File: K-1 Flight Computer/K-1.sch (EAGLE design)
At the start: 19 parts, among them IC1 BMP280, IC2 7805L, J1 1X2-3.5MM, J6 1X2-3.5MM, U1 MPU-6050-1

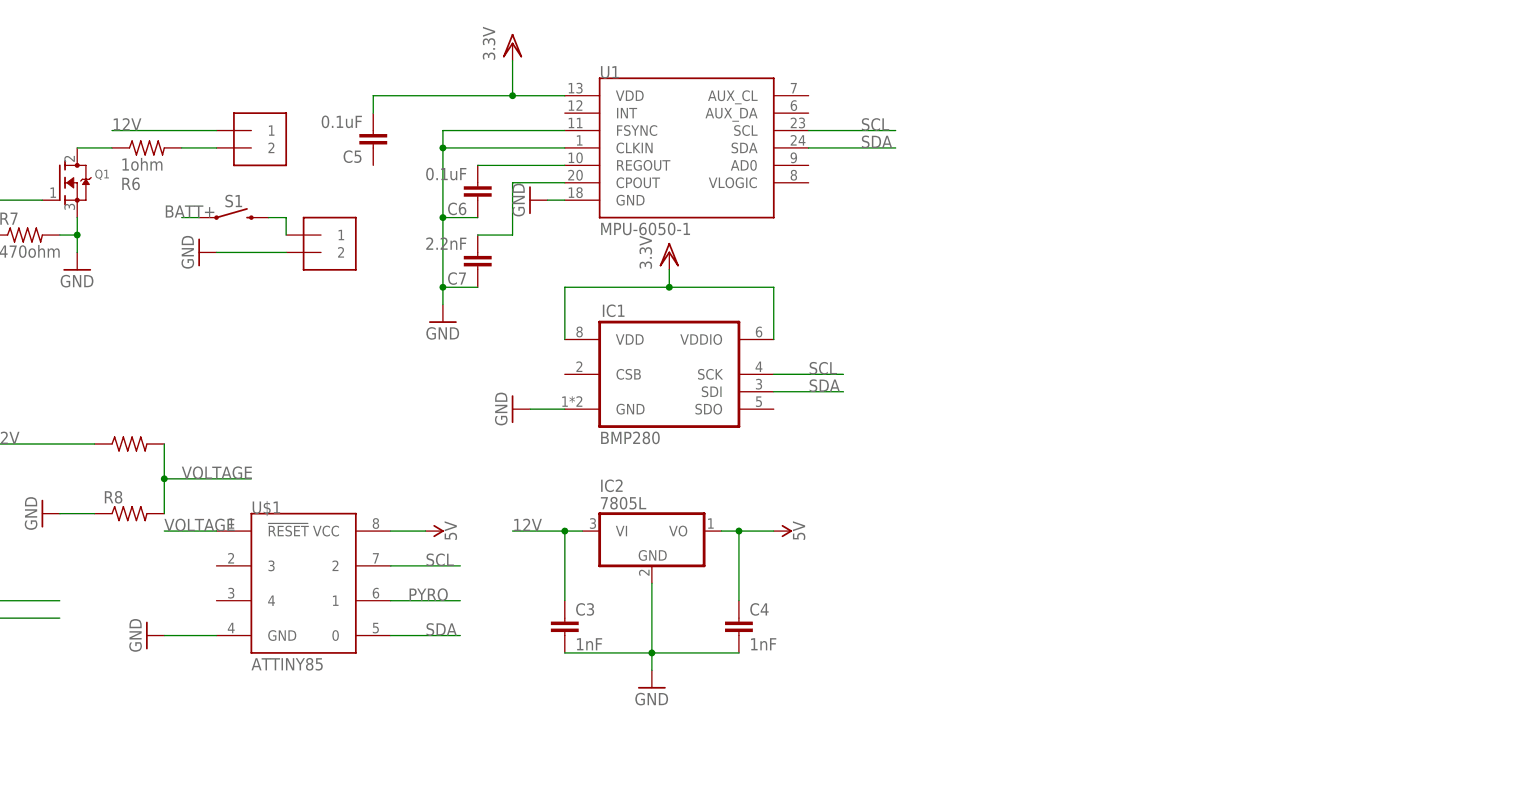
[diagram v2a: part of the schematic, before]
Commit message: Change MCU to STM32F103C8T7
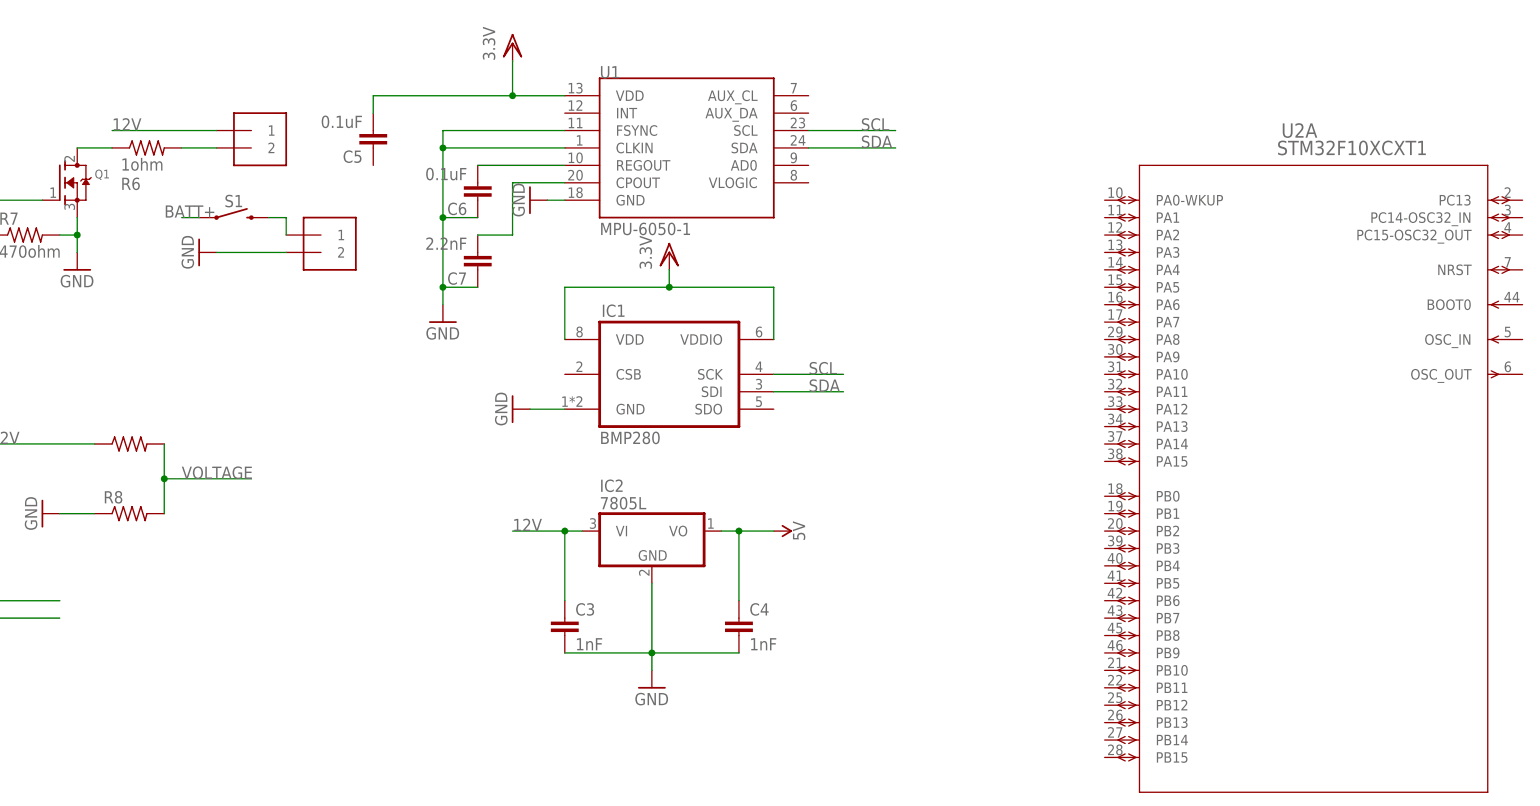
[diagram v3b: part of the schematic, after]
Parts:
- removed U$1: ATTINY85, attiny85:ATTINY85
- added U2: STM32F10XCXT1, STM32F103C8T7:STM32F10XCXT1
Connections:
- net 5V: no longer U$1.VCC
- net GND: no longer U$1.GND
- net PYRO: no longer U$1.1
- net SCL: no longer U$1.2
- net SDA: no longer U$1.0
- net VOLTAGE: no longer U$1.!RESET
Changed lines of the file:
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@@
 </classes>
 <parts>
-<part name="U$1" library="attiny85" deviceset="ATTINY85" device=""/>
 <part name="IC1" library="bosch-bmp280" deviceset="BMP280" device=""/>
 <part name="J1" library="adafruit" library_urn="urn:adsk.eagle:library:420" deviceset="1X2" device="-3.5MM" package3d_urn="urn:adsk.eagle:package:6240635/1"/>
@@
 <part name="R8" library="adafruit" library_urn="urn:adsk.eagle:library:420" deviceset="R-US_" device="0204/2V" package3d_urn="urn:adsk.eagle:package:6240630/1"/>
 <part name="GND8" library="supply1" library_urn="urn:adsk.eagle:library:371" deviceset="GND" device=""/>
-<part name="GND9" library="supply1" library_urn="urn:adsk.eagle:library:371" deviceset="GND" device=""/>
-<part name="SUPPLY2" library="SparkFun-PowerSymbols" library_urn="urn:adsk.eagle:library:530" deviceset="5V" device=""/>
 <part name="U1" library="Testing" deviceset="MPU-6050" device="-1"/>
 <part name="C3" library="capacitor-wima" library_urn="urn:adsk.eagle:library:116" deviceset="C" device="2,5-3" package3d_urn="urn:adsk.eagle:package:5436/1" value="1nF"/>
@@
 <part name="GND1" library="supply1" library_urn="urn:adsk.eagle:library:371" deviceset="GND" device=""/>
 <part name="S1" library="SparkFun-Switches" library_urn="urn:adsk.eagle:library:535" deviceset="MOMENTARY-SWITCH-SPST" device="-SMD-5.2-REDUNDANT" package3d_urn="urn:adsk.eagle:package:40167/1"/>
+<part name="U2" library="STM32F103C8T7" deviceset="STM32F10XCXT1" device=""/>
 </parts>
 <sheets>
@@
 </plain>
 <instances>
-<instance part="U$1" gate="G$1" x="142.24" y="78.74" smashed="yes">
-<attribute name="NAME" x="134.62" y="88.9" size="1.778" layer="95"/>
-<attribute name="VALUE" x="134.62" y="66.04" size="1.778" layer="96"/>
-</instance>
 <instance part="IC1" gate="G$1" x="195.58" y="109.22" smashed="yes">
 <attribute name="NAME" x="185.674" y="117.602" size="1.778" layer="95" font="vector"/>
@@
 <attribute name="VALUE" x="101.6" y="91.44" size="1.778" layer="96" rot="R270"/>
 </instance>
-<instance part="GND9" gate="1" x="119.38" y="71.12" smashed="yes" rot="R270">
-<attribute name="VALUE" x="116.84" y="73.66" size="1.778" layer="96" rot="R270"/>
-</instance>
-<instance part="SUPPLY2" gate="G$1" x="160.02" y="86.36" smashed="yes" rot="R270">
-<attribute name="VALUE" x="162.814" y="86.36" size="1.778" layer="96" rot="R270" align="bottom-center"/>
-</instance>
 <instance part="U1" gate="G$1" x="198.12" y="142.24" smashed="yes">
 <attribute name="NAME" x="185.42" y="152.4" size="1.778" layer="95"/>
@@
 <instance part="S1" gate="G$1" x="132.08" y="132.08" smashed="yes">
 <attribute name="NAME" x="132.08" y="133.604" size="1.778" layer="95" font="vector" align="bottom-center"/>
+</instance>
+<instance part="U2" gate="A" x="256.54" y="134.62" smashed="yes">
+<attribute name="NAME" x="284.8356" y="143.7386" size="2.0828" layer="95" ratio="6" rot="SR0"/>
+<attribute name="VALUE" x="284.2006" y="141.1986" size="2.0828" layer="96" ratio="6" rot="SR0"/>
 </instance>
 </instances>
@@
 <pinref part="GND8" gate="1" pin="GND"/>
 <wire x1="111.76" y1="88.9" x2="106.68" y2="88.9" width="0.1524" layer="91"/>
-</segment>
-<segment>
-<pinref part="U$1" gate="G$1" pin="GND"/>
-<wire x1="129.54" y1="71.12" x2="121.92" y2="71.12" width="0.1524" layer="91"/>
-<pinref part="GND9" gate="1" pin="GND"/>
 </segment>
 <segment>
@@
 <pinref part="C4" gate="G$1" pin="1"/>
 </segment>
-<segment>
-<pinref part="U$1" gate="G$1" pin="VCC"/>
-<pinref part="SUPPLY2" gate="G$1" pin="5V"/>
-<wire x1="154.94" y1="86.36" x2="160.02" y2="86.36" width="0.1524" layer="91"/>
-</segment>
 </net>
 <net name="N$4" class="0">
@@
 <label x="86.36" y="134.62" size="1.778" layer="95"/>
 </segment>
-<segment>
-<pinref part="U$1" gate="G$1" pin="1"/>
-<wire x1="154.94" y1="76.2" x2="165.1" y2="76.2" width="0.1524" layer="91"/>
-<label x="157.48" y="76.2" size="1.778" layer="95"/>
-</segment>
 </net>
 <net name="VOLTAGE" class="0">
@@
 <label x="124.46" y="93.98" size="1.778" layer="95"/>
 </segment>
-<segment>
-<pinref part="U$1" gate="G$1" pin="!RESET"/>
-<wire x1="129.54" y1="86.36" x2="121.92" y2="86.36" width="0.1524" layer="91"/>
-<label x="121.92" y="86.36" size="1.778" layer="95"/>
-</segment>
 </net>
 <net name="N$12" class="0">
@@
 </segment>
 <segment>
-<pinref part="U$1" gate="G$1" pin="0"/>
-<wire x1="154.94" y1="71.12" x2="165.1" y2="71.12" width="0.1524" layer="91"/>
-<label x="160.02" y="71.12" size="1.778" layer="95"/>
-</segment>
-<segment>
 <pinref part="U1" gate="G$1" pin="SDA"/>
 <wire x1="215.9" y1="142.24" x2="228.6" y2="142.24" width="0.1524" layer="91"/>
@@
 </segment>
 <segment>
-<pinref part="U$1" gate="G$1" pin="2"/>
-<wire x1="154.94" y1="81.28" x2="165.1" y2="81.28" width="0.1524" layer="91"/>
-<label x="160.02" y="81.28" size="1.778" layer="95"/>
-</segment>
-<segment>

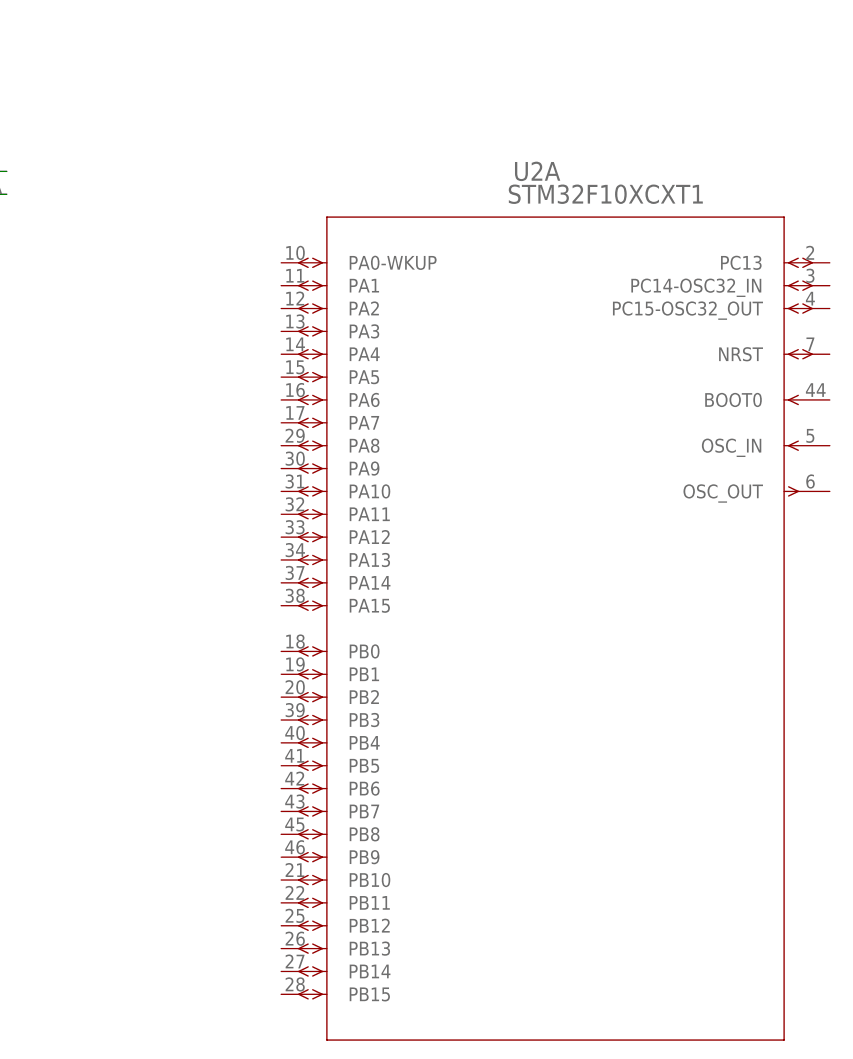
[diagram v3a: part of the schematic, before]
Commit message: Added custom MPU Eagle Library
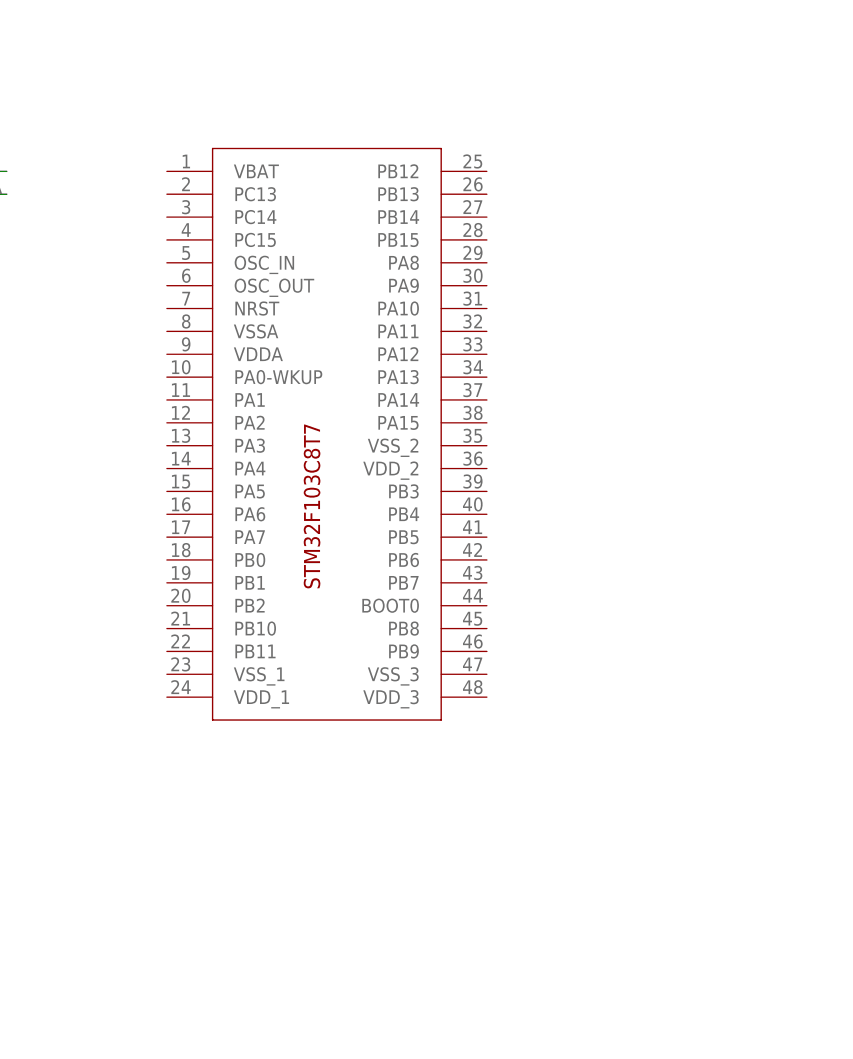
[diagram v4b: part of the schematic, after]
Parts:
- removed U2: STM32F10XCXT1, STM32F103C8T7:STM32F10XCXT1
- added U$1: STM32F103C8T7, STM32F103C8T7:STM32F103C8T7
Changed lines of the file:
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@@
 <part name="GND1" library="supply1" library_urn="urn:adsk.eagle:library:371" deviceset="GND" device=""/>
 <part name="S1" library="SparkFun-Switches" library_urn="urn:adsk.eagle:library:535" deviceset="MOMENTARY-SWITCH-SPST" device="-SMD-5.2-REDUNDANT" package3d_urn="urn:adsk.eagle:package:40167/1"/>
-<part name="U2" library="STM32F103C8T7" deviceset="STM32F10XCXT1" device=""/>
+<part name="U$1" library="STM32F103C8T7" deviceset="STM32F103C8T7" device=""/>
 </parts>
 <sheets>
@@
 <attribute name="NAME" x="132.08" y="133.604" size="1.778" layer="95" font="vector" align="bottom-center"/>
 </instance>
-<instance part="U2" gate="A" x="256.54" y="134.62" smashed="yes">
-<attribute name="NAME" x="284.8356" y="143.7386" size="2.0828" layer="95" ratio="6" rot="SR0"/>
-<attribute name="VALUE" x="284.2006" y="141.1986" size="2.0828" layer="96" ratio="6" rot="SR0"/>
-</instance>
+<instance part="U$1" gate="G$1" x="271.78" y="114.3" smashed="yes"/>
 </instances>
 <busses>

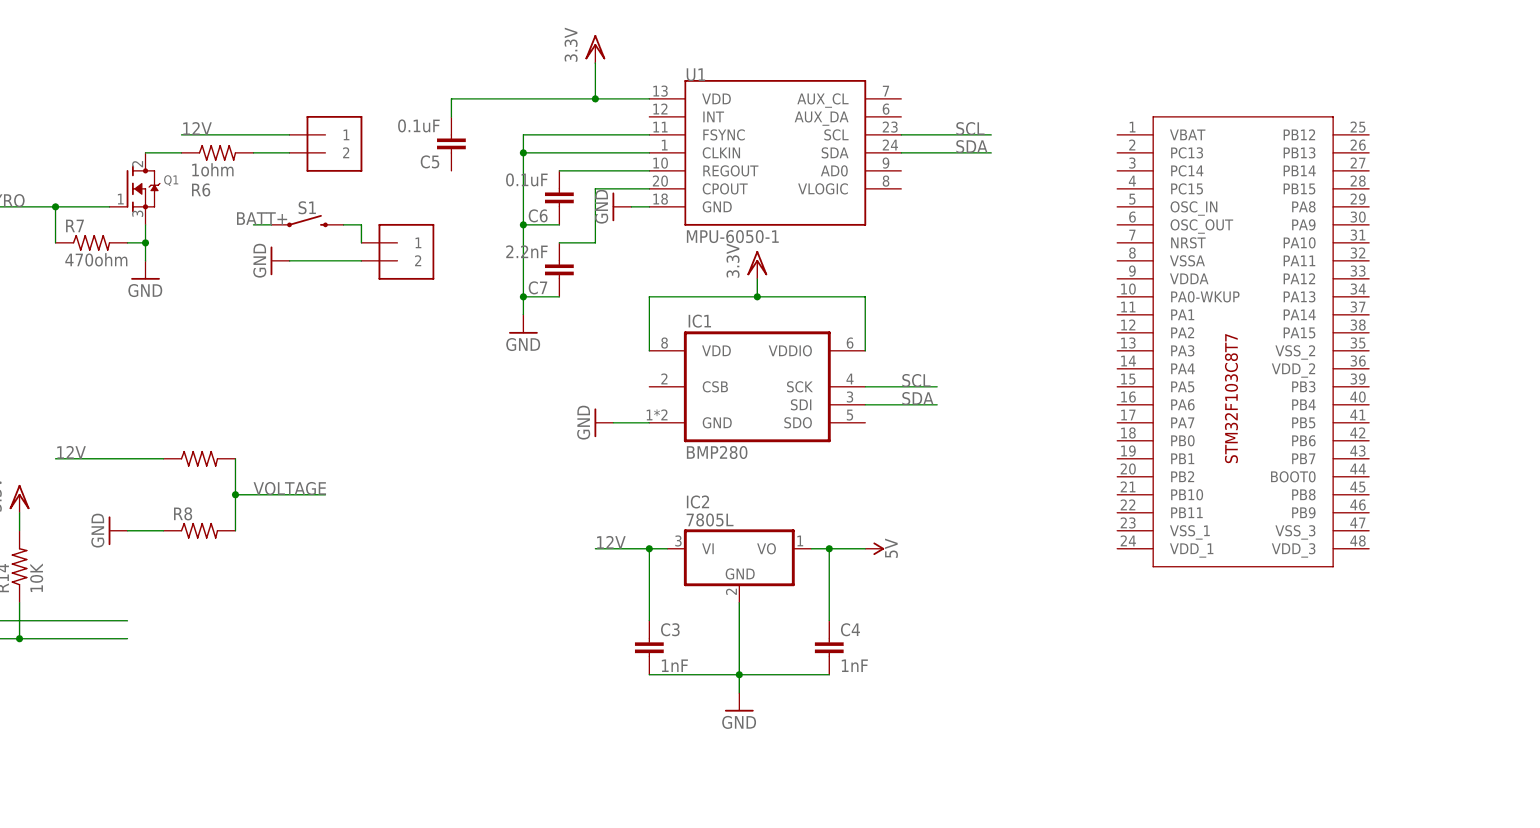
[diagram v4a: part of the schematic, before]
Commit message: Added W25Q32FV Memory Chip through SPI Protocol
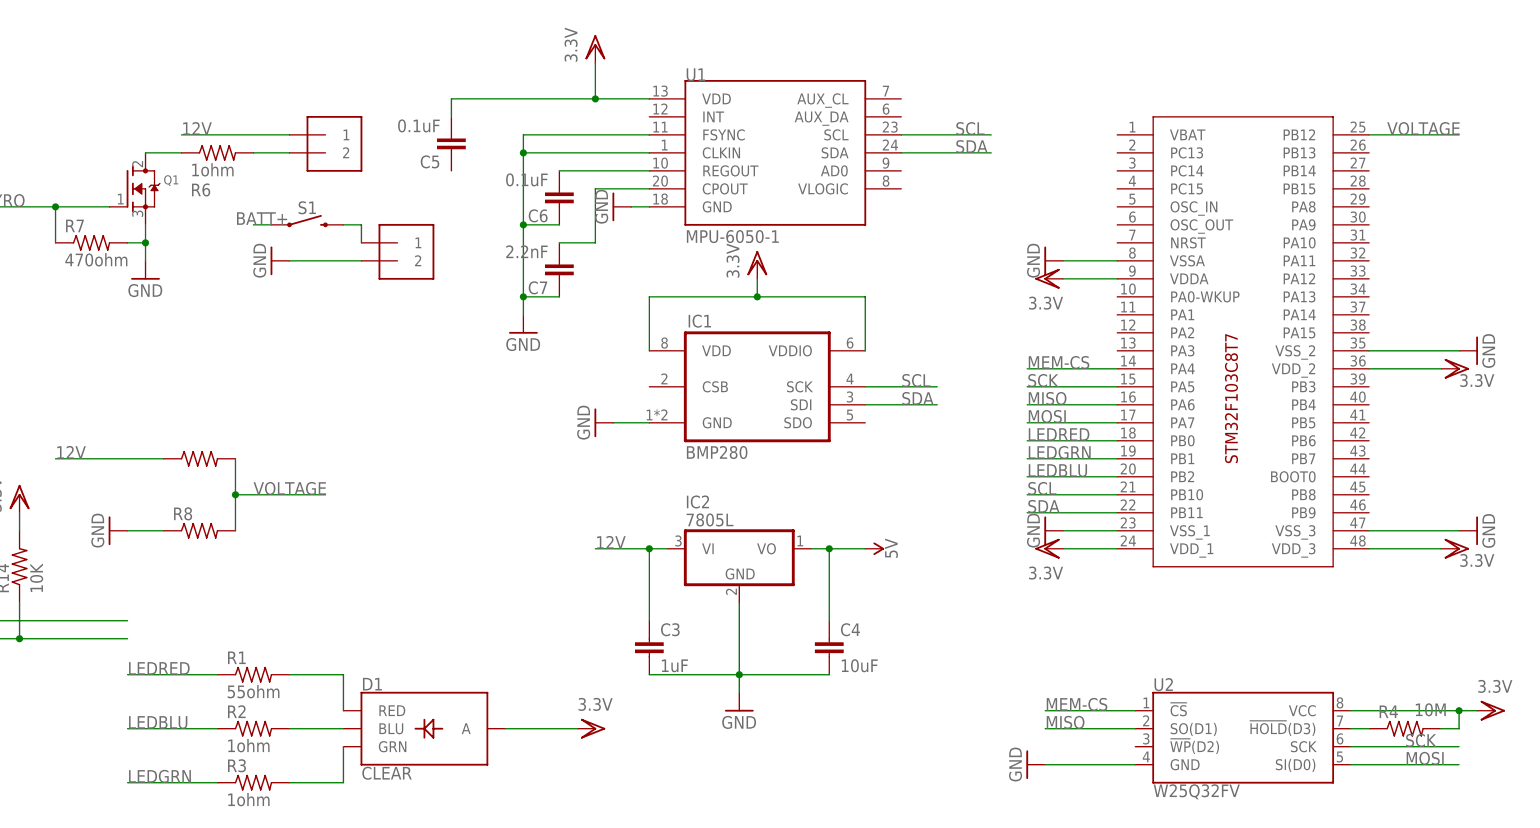
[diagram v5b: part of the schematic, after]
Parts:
- added D1: CLEAR, SparkFun-LED:LED-RGB-CACLEAR
- added R1: 55ohm, adafruit:R-US_0204/2V
- added R2, R3: 1ohm, adafruit:R-US_0204/2V
- added R4: 10M, adafruit:R-US_0204/2V
- added U2: W25Q32FV, SparkFun-IC-Memory:W25Q32FVSS
- C3: value 1nF -> 1uF
- C4: value 1nF -> 10uF
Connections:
- new net LEDBLU: R2.1, U$1.PB2
- new net LEDGRN: R3.1, U$1.PB1
- new net LEDRED: R1.1, U$1.PB0
- new net MEM-CS: U$1.PA4, U2.!CS!
- new net MISO: U$1.PA6, U2.SO(D1)
- new net MOSI: U$1.PA7, U2.SI(D0)
- new net N$1: D1.RED, R1.2
- new net N$2: D1.GRN, R3.2
- new net N$3: D1.BLU, R2.2
- new net N$5: R4.1, U2.!HOLD!(D3)
- new net SCK: U$1.PA5, U2.SCK
- net GND: now also U$1.VSSA, U$1.VSS_1, U$1.VSS_2, U$1.VSS_3, U2.GND
- net SCL: now also U$1.PB10
- net SDA: now also U$1.PB11
- net VDD: now also D1.A, R4.2, U$1.VDDA, U$1.VDD_1, U$1.VDD_2, U$1.VDD_3, U2.VCC
- net VOLTAGE: now also U$1.PB12
